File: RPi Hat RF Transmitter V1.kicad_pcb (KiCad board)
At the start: 4 copper layers, 65 x 56 mm, 67 parts, among them CON1 Sig_In, CON2 SMA-, CON3 Sig_In, CON4 Sig_In, CON5 SMA-, IC1 HMC241AQS16E, IC2 HMC241AQS16E, IC3 SN74HC139PW, J1 Conn_01x04_Male, J2 Conn_01x04_Male, J3 40HAT, J4 USB_B_Micro, J5 Conn_01x03_Male, J7 Conn_01x03_Male, U1 SBB5089Z, U2 74AUC2G04, X1 C, X10 L, X2 L, X3 C, X4 L, X5 C, X6 L, X7 C, X8 L, X9 C

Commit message: adds ufl connectors, now readymade filter at forth filter etc
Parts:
- removed CON3, CON4: Sig_In, Connector_Coaxial:SMA_Amphenol_132291-12_Vertical
- removed CON5: SMA-, Connector_Coaxial:SMA_Amphenol_132291-12_Vertical
- added C10: 22uF, Capacitor_SMD:C_1206_3216Metric_Pad1.42x1.75mm_HandSolder, F.Cu at (174.1, 59.2)
- added C12: 0.1uF, Capacitor_SMD:C_0805_2012Metric_Pad1.15x1.40mm_HandSolder, F.Cu at (173.5, 62.3)
- added C18: 22uF, Capacitor_SMD:C_1206_3216Metric_Pad1.42x1.75mm_HandSolder, F.Cu at (179.6, 52.8)
- added C2: 10uF, Capacitor_SMD:C_0805_2012Metric_Pad1.15x1.40mm_HandSolder, F.Cu at (179.4, 58.9)
- added C4: 0.1uF, Capacitor_SMD:C_0805_2012Metric_Pad1.15x1.40mm_HandSolder, F.Cu at (179.0, 55.9)
- added C6: 10uF, Capacitor_SMD:C_1206_3216Metric_Pad1.42x1.75mm_HandSolder, F.Cu at (179.6, 49.5)
- added C8: 10uF, Capacitor_SMD:C_0805_2012Metric_Pad1.15x1.40mm_HandSolder, F.Cu at (185.0, 49.4)
- added FIL4: LFCN-180, Filter:Filter_Mini-Circuits_FV1206, F.Cu at (165.1, 67.1)
- added IC4: ADG904BRUZ-R, SamacSys_Parts:SOP65P640X120-20N, F.Cu at (236.7, 71.1)
- added J10: U.FL-R-SMT(10), SamacSys_Parts:UFLRSMT10, F.Cu at (215.9, 62.1)
- added J11: U.FL-R-SMT(10), SamacSys_Parts:UFLRSMT10, F.Cu at (222.7, 56.2)
- added J12: U.FL-R-SMT(10), SamacSys_Parts:UFLRSMT10, F.Cu at (222.7, 62.1)
- added J6: Conn_01x03_Male, Connector_PinHeader_2.54mm:PinHeader_1x03_P2.54mm_Vertical, F.Cu at (169.7, 50.2)
- added J8: Conn_01x03_Male, Connector_PinHeader_2.54mm:PinHeader_1x03_P2.54mm_Vertical, F.Cu at (174.3, 50.2)
- added J9: U.FL-R-SMT(10), SamacSys_Parts:UFLRSMT10, F.Cu at (215.9, 56.2)
- added JP5: Jumper, Connector_PinHeader_2.54mm:PinHeader_1x02_P2.54mm_Vertical, F.Cu at (184.2, 72.1)
- added JP6: Jumper, Connector_PinHeader_2.54mm:PinHeader_1x02_P2.54mm_Vertical, F.Cu at (168.8, 59.9)
- added R1: 330, Resistor_SMD:R_0805_2012Metric_Pad1.15x1.40mm_HandSolder, F.Cu at (185.0, 52.3)
- added R2: 10K, Resistor_SMD:R_0805_2012Metric_Pad1.15x1.40mm_HandSolder, F.Cu at (170.4, 66.3)
- added R3: 330, Resistor_SMD:R_0805_2012Metric_Pad1.15x1.40mm_HandSolder, F.Cu at (183.8, 55.9)
- added R4: 330, Resistor_SMD:R_0805_2012Metric_Pad1.15x1.40mm_HandSolder, F.Cu at (170.4, 69.2)
- added R5: 10K, Resistor_SMD:R_0805_2012Metric_Pad1.15x1.40mm_HandSolder, F.Cu at (189.7, 49.4)
- added R7: 120, Resistor_SMD:R_0805_2012Metric_Pad1.15x1.40mm_HandSolder, F.Cu at (178.2, 62.3)
- added R8: 120, Resistor_SMD:R_0805_2012Metric_Pad1.15x1.40mm_HandSolder, F.Cu at (184.2, 58.9)
- added R9: 330, Resistor_SMD:R_0805_2012Metric_Pad1.15x1.40mm_HandSolder, F.Cu at (189.7, 52.3)
- C1, C5: value C -> 62pF
- C3: value C -> 3.3pF
- D1: value LED -> Blue
- D2: value LED -> Green
- D3: value LED -> Orange
- D4: value LED -> Yellow
- D5, D6, D7: value LED -> Red
- IC1: value HMC241AQS16E -> ADG904BRUZ-R; footprint SamacSys_Parts:SOP64P600X175-16N -> SamacSys_Parts:SOP65P640X120-20N
- IC2: value HMC241AQS16E -> SN74HC139PW; footprint SamacSys_Parts:SOP64P600X175-16N -> Package_SO:TSSOP-16_4.4x5mm_P0.65mm
- J1: value Conn_01x04_Male -> Conn_01x08_Male; footprint Connector_PinHeader_2.54mm:PinHeader_1x04_P2.54mm_Vertical -> Connector_PinHeader_2.54mm:PinHeader_1x08_P2.54mm_Vertical
- L1, L5: value L -> 18nH
- L3: value L -> 330nH
- R15: moved to F.Cu
- U2: value 74AUC2G04 -> LM1117-ADJ; footprint Package_TO_SOT_SMD:SOT-23-6_Handsoldering -> Package_TO_SOT_SMD:SOT-223-3_TabPin2
- moved IC1 135.7 mm to (227.1, 71.0), turned to 0 degrees
- moved J1 111.8 mm to (199.9, 50.9)
- moved R15 76.9 mm to (175.1, 65.3)
- moved U2 56.3 mm to (162.4, 52.0)
- moved IC2 45.2 mm to (162.0, 59.6), turned to 0 degrees
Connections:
- net /P5V_HAT renamed Net-(J3-Pad2)
- C1 pad 1: RF1_OUT -> FIL_IN_1
- C11 pad 1: RF2_IN -> FIL_OUT_2
- C13 pad 1: RF_ANT_OUT -> Net-(C13-Pad1)
- C19 pad 1: RF_SWITCH_PWR -> DECODER_PWR
- C3 pad 1: RF1_OUT -> FIL_IN_1
- C5 pad 1: RF1_IN -> FIL_OUT_1
- C7 pad 1: RF2_OUT -> FIL_IN_2
- C9 pad 1: RF2_OUT -> FIL_IN_2
- CON1 pad 1: GPIO4 -> Net-(CON1-Pad1)
- D7 pad 1: Net-(D7-Pad1) -> GND
- IC1 pad 1: GPIO4 -> Net-(IC1-Pad1)
- IC1 pad 10: GPIO27 -> Net-(CON1-Pad1)
- IC1 pad 12: RF2_OUT -> GND
- IC1 pad 14: RF1_OUT -> FIL_IN_4
- IC1 pad 2: GND -> RF_SWITCH_PWR
- IC1 pad 4: RF4_OUT -> FIL_IN_2
- IC1 pad 6: RF3_OUT -> GND
- IC1 pad 7: GND -> FIL_IN_1
- IC1 pad 8: RF_SWITCH_PWR -> GND
- IC1 pad 9: GPIO17 -> GND
- IC2 pad 1: RF_ANT_OUT -> DECODER_EN
- IC2 pad 11: GND -> Net-(IC2-Pad11)
- IC2 pad 12: RF3_IN -> Net-(IC2-Pad12)
- IC2 pad 13: GND -> Net-(IC2-Pad13)
- IC2 pad 14: RF4_IN -> Net-(IC2-Pad14)
- IC2 pad 15: GND -> Net-(IC2-Pad15)
- IC2 pad 16: GND -> DECODER_PWR
- IC2 pad 2: GND -> A0_1
- IC2 pad 3: GND -> A1_1
- IC2 pad 4: RF1_IN -> SEL_RF1
- IC2 pad 5: GND -> SEL_RF2
- IC2 pad 6: RF2_IN -> SEL_RF3
- IC2 pad 7: GND -> SEL_RF4
- IC2 pad 8: RF_SWITCH_PWR -> GND
- IC3 pad 1: GPIO22 -> DECODER_EN
- IC3 pad 16: RF_SWITCH_PWR -> DECODER_PWR
- IC3 pad 2: GPIO17 -> A0_1
- IC3 pad 3: GPIO27 -> A1_1
- J1 pad 1: GPIO17 -> GND
- J1 pad 2: GPIO27 -> +5V
- J1 pad 3: +5V -> A1_2
- J1 pad 4: GND -> A0_2
- J2 pad 1: +5V -> GND
- J2 pad 2: +5V -> GND
- J2 pad 3: GND -> +5V
- J2 pad 4: GND -> +5V
- J3 pad 11: GPIO17 -> A0_1
- J3 pad 13: GPIO27 -> A1_1
- J3 pad 15: GPIO22 -> RF_SWITCH_EN
- J3 pad 17: Net-(J3-Pad17) -> A0_2
- J3 pad 19: Net-(J3-Pad19) -> A1_2
- J3 pad 23: Net-(J3-Pad23) -> DECODER_EN
- J3 pad 7: GPIO4 -> RPI_RF_OUT
- J5 pad 1: +5V -> RF_SWITCH_PWR
- J5 pad 2: GPIO17 -> A0_1_JMP
- J7 pad 1: +5V -> RF_SWITCH_PWR
- J7 pad 2: GPIO27 -> A1_1_JMP
- JP2 pad 2: RF_SWITCH_PWR -> DECODER_PWR
- JP3 pad 2: GPIO22 -> DECODER_EN
- L1 pad 1: RF1_OUT -> FIL_IN_1
- L11 pad 1: RF2_IN -> FIL_OUT_2
- L3 pad 2: RF1_IN -> FIL_OUT_1
- L5 pad 1: RF1_IN -> FIL_OUT_1
- L7 pad 1: RF2_OUT -> FIL_IN_2
- L9 pad 2: RF2_IN -> FIL_OUT_2
- R15 pad 1: GND -> A1_2
- R15 pad 2: Net-(D7-Pad1) -> A1_2_JMP
- U2 pad 1: GPIO17 -> Net-(C10-Pad1)
- U2 pad 2: GND -> RF_SWITCH_PWR
- U2 pad 3: GPIO27 -> DECODER_PWR
- X1 pad 1: RF3_OUT -> FIL_IN_3
- X10 pad 1: RF3_IN -> FIL_OUT_3
- X2 pad 1: RF3_OUT -> FIL_IN_3
- X3 pad 1: RF3_OUT -> FIL_IN_3
- X8 pad 2: RF3_IN -> FIL_OUT_3
- X9 pad 1: RF3_IN -> FIL_OUT_3
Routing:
- net GPIO27: track 118.1 -> 0.00 mm, vias 4 -> 0
- net +5V: track 121.2 -> 16.0 mm
- net GPIO17: track 94.4 -> 0.00 mm, vias 1 -> 0
- net RF_SWITCH_PWR: track 70.4 -> 0.27 mm, vias 5 -> 0
- net GPIO22: track 52.1 -> 0.00 mm, vias 1 -> 0
- net GPIO4: track 37.8 -> 0.00 mm
- net GND: track 91.6 -> 61.4 mm, vias 399 -> 238
- net RF_ANT_OUT: track 22.8 -> 0.00 mm
- net RF1_OUT: track 22.8 -> 0.00 mm
- net RF1_IN: track 22.4 -> 0.00 mm
- net RF4_IN: track 18.7 -> 0.00 mm
- net RF4_OUT: track 17.6 -> 0.00 mm
- net RF2_OUT: track 15.6 -> 0.00 mm
- net RF2_IN: track 15.1 -> 0.00 mm
- net Net-(IC2-Pad10): track 12.1 -> 0.00 mm
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
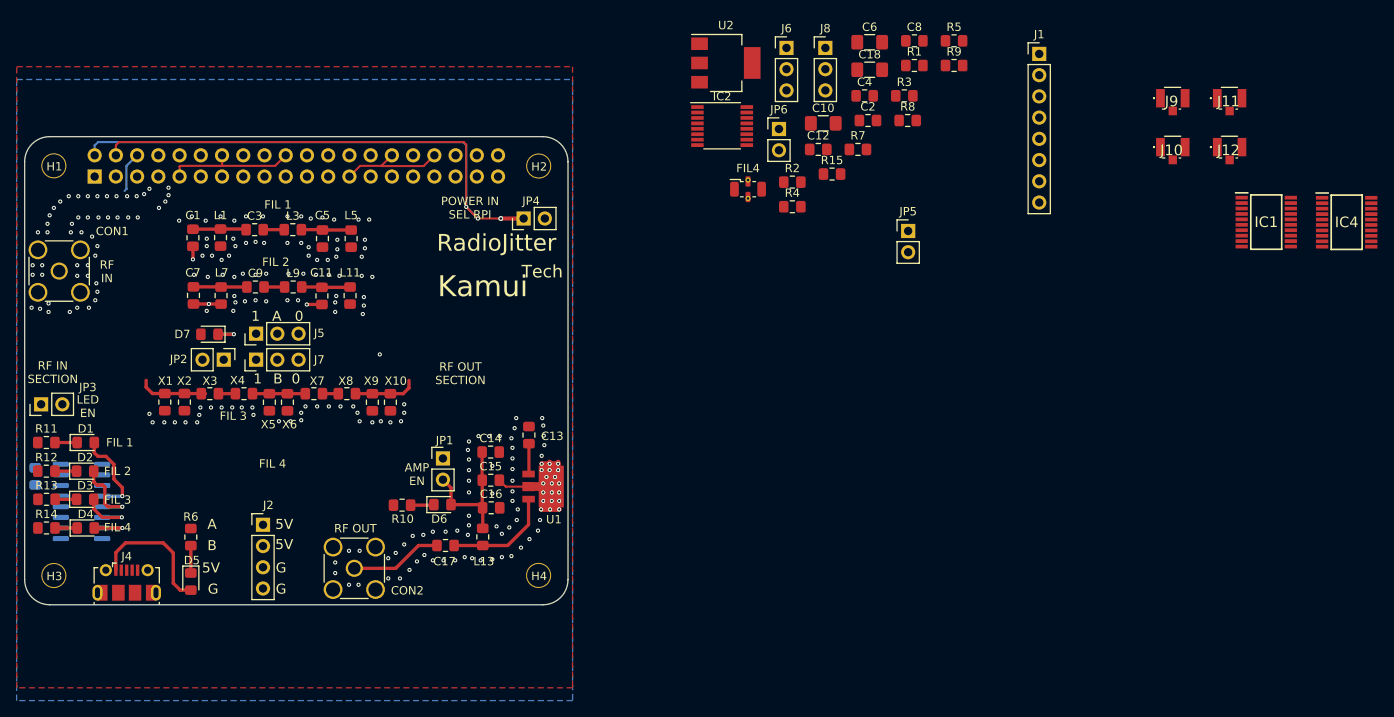
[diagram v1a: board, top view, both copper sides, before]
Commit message: routed for new circuit
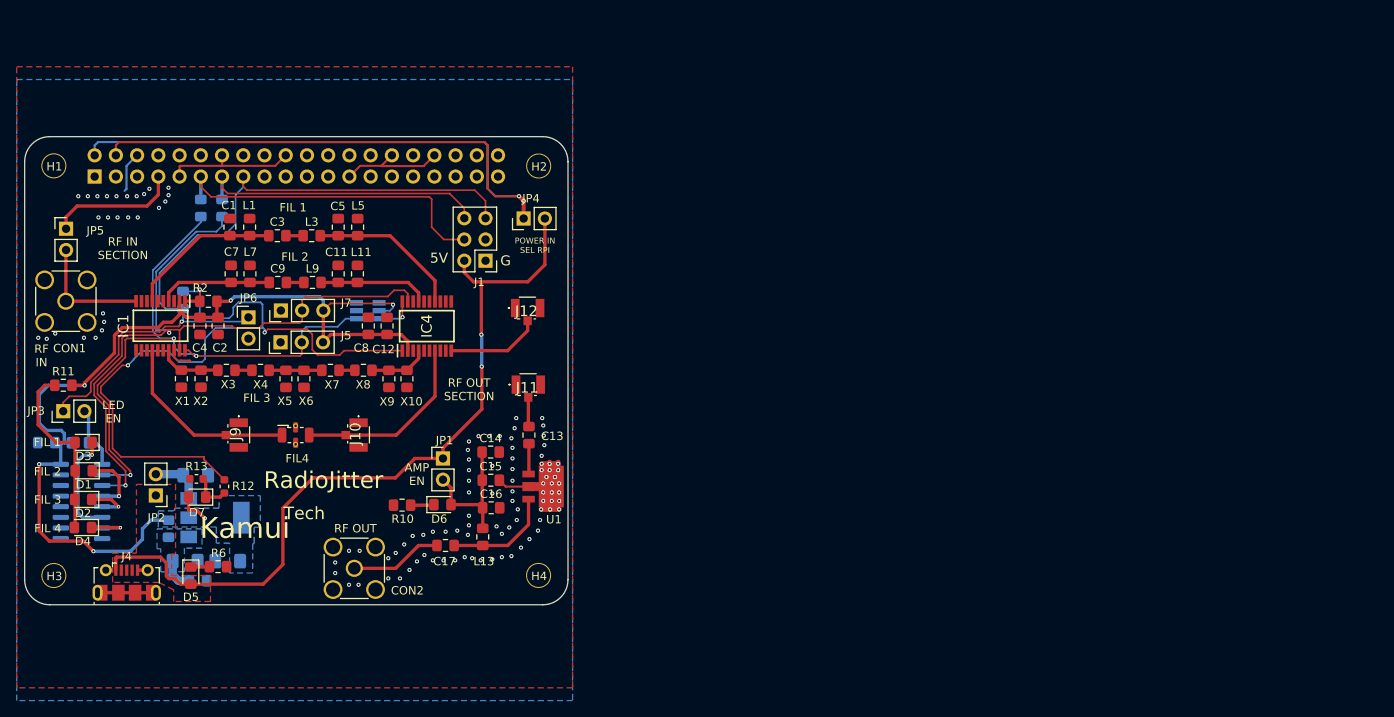
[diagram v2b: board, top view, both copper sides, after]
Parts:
- removed IC2: SN74HC139PW, Package_SO:TSSOP-16_4.4x5mm_P0.65mm
- removed J2: Conn_01x04_Male, Connector_PinHeader_2.54mm:PinHeader_1x04_P2.54mm_Vertical
- removed J6, J8: Conn_01x03_Male, Connector_PinHeader_2.54mm:PinHeader_1x03_P2.54mm_Vertical
- removed R14, R15, R9: 330, Resistor_SMD:R_0805_2012Metric_Pad1.15x1.40mm_HandSolder
- added U3: 74AUC2G04, Package_TO_SOT_SMD:SOT-23-6_Handsoldering, B.Cu at (119.6, 81.6)
- C10, C18, C6, R1, R3, R4, R5, R7, R8, U2: moved to B.Cu
- J1: value Conn_01x08_Male -> Conn_02x03_Odd_Even; footprint Connector_PinHeader_2.54mm:PinHeader_1x08_P2.54mm_Vertical -> Connector_PinHeader_2.54mm:PinHeader_2x03_P2.54mm_Vertical
- R12, R13: value 330 -> DNP; footprint Resistor_SMD:R_0805_2012Metric_Pad1.15x1.40mm_HandSolder -> Resistor_SMD:R_0603_1608Metric
- moved IC1 132.9 mm to (94.8, 83.4), turned to 270 degrees
- moved J9 118.8 mm to (104.2, 96.5), turned to 270 degrees
- moved R5 115.1 mm to (85.2, 97.4), turned to 180 degrees
- moved IC4 110.7 mm to (126.7, 83.5), turned to 90 degrees
- moved J10 103.3 mm to (118.5, 96.5), turned to 270 degrees
- moved R8 101.0 mm to (95.8, 107.7), turned to 270 degrees
- moved JP5 100.7 mm to (83.5, 71.8)
- moved C18 96.7 mm to (102.8, 111.6), turned to 180 degrees
- moved C6 95.8 mm to (99.0, 101.3)
- moved R7 94.3 mm to (99.3, 113.9), turned to 180 degrees
- moved C10 92.6 mm to (97.7, 111.6)
- moved R1 91.9 mm to (97.5, 80.4), turned to 270 degrees
- moved J11 90.6 mm to (138.8, 90.5)
- moved J12 86.2 mm to (138.7, 81.3)
- moved R3 85.2 mm to (99.6, 69.4), turned to 270 degrees
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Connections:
- C19 pad 1: DECODER_PWR -> RF_SWITCH_PWR
- C6 pad 1: DECODER_PWR -> Net-(C6-Pad1)
- D1 pad 1: Net-(D1-Pad1) -> SEL_RF1
- D1 pad 2: SEL_RF1 -> Net-(D1-Pad2)
- D2 pad 1: Net-(D2-Pad1) -> SEL_RF2
- D2 pad 2: SEL_RF2 -> Net-(D1-Pad2)
- D3 pad 1: Net-(D3-Pad1) -> SEL_RF3
- D3 pad 2: SEL_RF3 -> Net-(D1-Pad2)
- D4 pad 1: Net-(D4-Pad1) -> SEL_RF4
- D4 pad 2: SEL_RF4 -> Net-(D1-Pad2)
- D7 pad 1: GND -> Net-(D7-Pad1)
- IC1 pad 1: Net-(IC1-Pad1) -> RF_SWITCH_EN_STATUS
- IC1 pad 19: A1_1_JMP -> A1_JMP
- IC1 pad 20: A0_1_JMP -> A0_JMP
- IC3 pad 1: DECODER_EN -> Net-(IC3-Pad1)
- IC3 pad 16: DECODER_PWR -> RF_SWITCH_PWR
- IC3 pad 2: A0_1 -> A0_JMP
- IC3 pad 3: A1_1 -> A1_JMP
- IC4 pad 1: Net-(IC1-Pad1) -> RF_SWITCH_EN_STATUS
- IC4 pad 19: A1_2_JMP -> A1_JMP
- IC4 pad 20: A0_2_JMP -> Net-(IC4-Pad20)
- J1 pad 3: A1_2 -> Net-(J1-Pad3)
- J1 pad 4: A0_2 -> A0_RPI
- J1 pad 5: A1_1 -> RF_SWITCH_EN
- J1 pad 6: A0_1 -> A1_RPI
- J3 pad 11: A0_1 -> A0_RPI
- J3 pad 13: A1_1 -> A1_RPI
- J3 pad 17: A0_2 -> Net-(J3-Pad17)
- J3 pad 19: A1_2 -> Net-(J3-Pad19)
- J3 pad 23: DECODER_EN -> Net-(J3-Pad23)
- J5 pad 1: RF_SWITCH_PWR -> GND
- J5 pad 2: A0_1_JMP -> A0_JMP
- J5 pad 3: GND -> RF_SWITCH_PWR
- J7 pad 1: RF_SWITCH_PWR -> GND
- J7 pad 2: A1_1_JMP -> A1_JMP
- J7 pad 3: GND -> RF_SWITCH_PWR
- JP2 pad 2: DECODER_PWR -> Net-(C6-Pad1)
- JP3 pad 1: GND -> RF_SWITCH_EN
- JP3 pad 2: DECODER_EN -> Net-(IC3-Pad1)
- R1 pad 1: Net-(IC1-Pad1) -> RF_SWITCH_EN_STATUS
- R11 pad 1: GND -> Net-(D1-Pad2)
- R11 pad 2: Net-(D1-Pad1) -> RF_SWITCH_PWR
- R12 pad 1: GND -> RF_SWITCH_EN_STATUS
- R12 pad 2: Net-(D2-Pad1) -> Net-(D7-Pad1)
- R13 pad 2: Net-(D3-Pad1) -> Net-(D7-Pad1)
- R2 pad 2: Net-(IC1-Pad1) -> RF_SWITCH_EN_STATUS
- R3 pad 1: A0_1 -> A0_RPI
- R3 pad 2: A0_1_JMP -> A0_JMP
- R4 pad 1: A1_1 -> A1_RPI
- R4 pad 2: A1_1_JMP -> A1_JMP
- R5 pad 1: DECODER_EN -> Net-(IC3-Pad1)
- R5 pad 2: DECODER_PWR -> RF_SWITCH_PWR
- U2 pad 3: DECODER_PWR -> Net-(C6-Pad1)
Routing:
- net RF_SWITCH_PWR: track 0.27 -> 119.4 mm, vias 0 -> 6
- net RF_SWITCH_EN: track 0.00 -> 88.3 mm, vias 0 -> 1
- net RF_SWITCH_EN_STATUS: track 0.00 -> 88.0 mm, vias 0 -> 3
- net A1_JMP: track 0.00 -> 85.4 mm, vias 0 -> 2
- net +5V: track 16.0 -> 94.1 mm, vias 0 -> 2
- net A0_JMP: track 0.00 -> 75.8 mm, vias 0 -> 3
- net A0_RPI: track 0.00 -> 40.1 mm
- net A1_RPI: track 0.00 -> 35.3 mm
- net FIL_IN_4: track 0.00 -> 22.7 mm
- net FIL_OUT_4: track 0.00 -> 22.5 mm
- net Net-(D1-Pad2): track 0.00 -> 21.7 mm
- net RPI_RF_OUT: track 0.00 -> 15.7 mm
- net Net-(CON1-Pad1): track 0.00 -> 14.5 mm
- net FIL_OUT_1: track 5.97 -> 18.5 mm
- net FIL_IN_1: track 6.40 -> 18.4 mm
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- added copper zone on F.Cu, net +5V
- added copper zone on B.Cu, net Net-(C10-Pad1)
- added copper zone on B.Cu, net RF_SWITCH_PWR
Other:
- net class Default: trace_width 0.15 -> 0.2
